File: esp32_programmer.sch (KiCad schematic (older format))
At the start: 5 parts

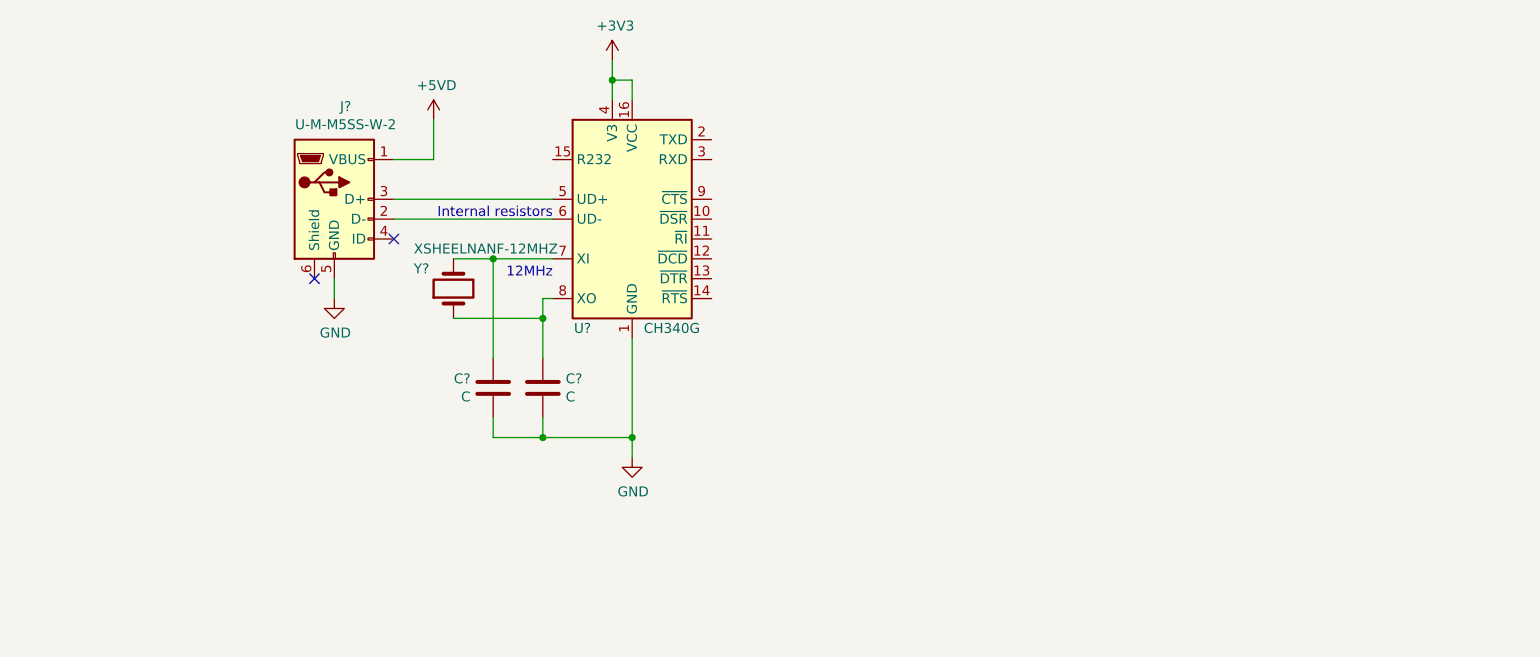
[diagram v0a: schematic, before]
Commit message: corrected capacitors
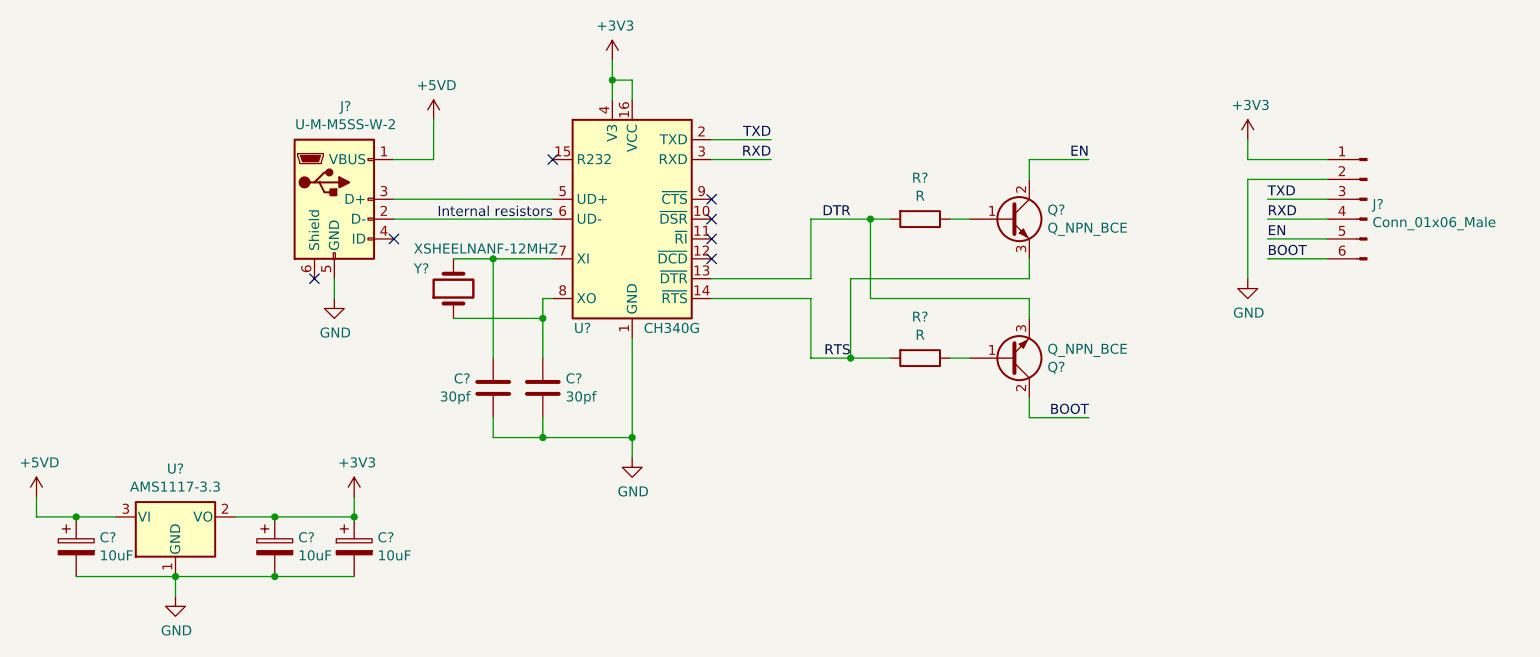
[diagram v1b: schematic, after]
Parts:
- added C? (x3): 10uF, symbol Device:CP
- added J?: Conn_01x06_Male, symbol Connector:Conn_01x06_Male
- added Q? (x2): Q_NPN_BCE, symbol Device:Q_NPN_BCE
- added R? (x2): R, symbol Device:R
- added U?: AMS1117-3.3, Package_TO_SOT_SMD:SOT-223-3_TabPin2, symbol Regulator_Linear:AMS1117-3.3
- C? (x2): value C -> 30pf
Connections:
- net +3V3: now also C?.1, C?.1, J?.1 (Pin_1), U?.2 (VO)
- net +5VD: now also C?.1, U?.3 (VI)
- net GND: now also C?.2, C?.2, C?.2, J?.2 (Pin_2), U?.1 (GND)
- net DTR: now reaches U?.13 (~DTR)
- net DTR: now also Q?.3 (E), R?.2
- net RTS: now reaches U?.14 (~RTS)
- net RTS: now also Q?.3 (E), R?.2
- net TXD: now reaches U?.2 (TXD)
- net TXD: now also J?.3 (Pin_3)
- net RXD: now reaches U?.3 (RXD)
- net RXD: now also J?.4 (Pin_4)
- new net: Q?.1 (B), R?.1 (x2)
- new net BOOT: J?.6 (Pin_6), Q?.2 (C)
- new net EN: J?.5 (Pin_5), Q?.2 (C)
- no-connect marks 2 -> 7
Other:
- note removed: "12MHz"

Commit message: Add project footprints and route PCB
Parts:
- C1, C2, C3: renamed from C?; footprint (none) -> Capacitor_Tantalum_SMD:CP_EIA-3216-18_Kemet-A
- C4, C5: renamed from C?; footprint (none) -> Capacitor_SMD:C_0603_1608Metric
- J1: renamed from J?; value U-M-M5SS-W-2 -> MicroQTJ; footprint (none) -> esp32-programmer:USB_MicroQTJ; LCSC https://lcsc.com/product-detail/USB-Connectors_Korean-Hropa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 -> https://lcsc.com/product-detail/USB-Connectors_SHOU-HAN-Mic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
- J2: renamed from J?; footprint (none) -> Connector_PinHeader_2.54mm:PinHeader_1x06_P2.54mm_Vertical
- Q1, Q2: renamed from Q?; footprint (none) -> Package_TO_SOT_SMD:SOT-23
- R1, R2: renamed from R?; footprint (none) -> Resistor_SMD:R_0603_1608Metric
- Y1: renamed from Y?; footprint (none) -> esp32-programmer:XTAL_XSHEELNANF-12MHZ
- gave numbers to parts that had none: 2
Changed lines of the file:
@@
 $EndDescr
 $Comp
-L Interface_USB:CH340G U?
+L Interface_USB:CH340G U2
 U 1 1 60B77A02
 P 5300 3500
-F 0 "U?" H 5050 2950 50  0000 C CNN
+F 0 "U2" H 5050 2950 50  0000 C CNN
 F 1 "CH340G" H 5500 2950 50  0000 C CNN
 F 2 "Package_SO:SOIC-16_3.9x9.9mm_P1.27mm" H 5350 2950 50  0001 L CNN
@@
 $EndComp
 $Comp
-L Connector:USB_B_Micro J?
+L Connector:USB_B_Micro J1
 U 1 1 60B78CA0
 P 3800 3400
-F 0 "J?" H 3857 3867 50  0000 C CNN
-F 1 "U-M-M5SS-W-2" H 3857 3776 50  0000 C CNN
-F 2 "" H 3950 3350 50  0001 C CNN
+F 0 "J1" H 3857 3867 50  0000 C CNN
+F 1 "MicroQTJ" H 3857 3776 50  0000 C CNN
+F 2 "esp32-programmer:USB_MicroQTJ" H 3950 3350 50  0001 C CNN
 F 3 "~" H 3950 3350 50  0001 C CNN
-F 4 "https://lcsc.com/product-detail/USB-Connectors_Korean-Hroparts-Elec-U-M-M5SS-W-2_C91144.html/?href=jlc-SMT" H 3800 3400 50  0001 C CNN "LCSC"
+F 4 "https://lcsc.com/product-detail/USB-Connectors_SHOU-HAN-MicroQTJ_C404968.html/?href=jlc-SMT" H 3800 3400 50  0001 C CNN "LCSC"
 	1    3800 3400
 	1    0    0    -1
@@
 Internal resistors
 $Comp
-L Device:Crystal Y?
+L Device:Crystal Y1
 U 1 1 60B7C29D
 P 4400 3850
-F 0 "Y?" V 4500 4050 50  0000 R CNN
+F 0 "Y1" V 4500 4050 50  0000 R CNN
 F 1 "XSHEELNANF-12MHZ" V 4600 4050 50  0000 R CNN
-F 2 "" H 4400 3850 50  0001 C CNN
+F 2 "esp32-programmer:XTAL_XSHEELNANF-12MHZ" H 4400 3850 50  0001 C CNN
 F 3 "~" H 4400 3850 50  0001 C CNN
 	1    4400 3850
@@
 	3800 3800 3800 3900
 $Comp
-L power:GND #PWR?
+L power:GND #PWR0101
 U 1 1 60B7FF57
 P 3800 3900
-F 0 "#PWR?" H 3800 3650 50  0001 C CNN
+F 0 "#PWR0101" H 3800 3650 50  0001 C CNN
 F 1 "GND" H 3805 3727 50  0000 C CNN
 F 2 "" H 3800 3900 50  0001 C CNN
@@
 	4300 3200 4300 3000
 $Comp
-L power:+5VD #PWR?
+L power:+5VD #PWR0102
 U 1 1 60B80375
 P 4300 3000
-F 0 "#PWR?" H 4300 2850 50  0001 C CNN
+F 0 "#PWR0102" H 4300 2850 50  0001 C CNN
 F 1 "+5VD" H 4315 3173 50  0000 C CNN
 F 2 "" H 4300 3000 50  0001 C CNN
@@
 $EndComp
 $Comp
-L power:+3V3 #PWR?
+L power:+3V3 #PWR0103
 U 1 1 60B80565
 P 5200 2700
-F 0 "#PWR?" H 5200 2550 50  0001 C CNN
+F 0 "#PWR0103" H 5200 2550 50  0001 C CNN
 F 1 "+3V3" H 5215 2873 50  0000 C CNN
 F 2 "" H 5200 2700 50  0001 C CNN
@@
 	5200 2800 5200 2900
 $Comp
-L power:GND #PWR?
+L power:GND #PWR0104
 U 1 1 60B80D8B
 P 5300 4700
-F 0 "#PWR?" H 5300 4450 50  0001 C CNN
+F 0 "#PWR0104" H 5300 4450 50  0001 C CNN
 F 1 "GND" H 5305 4527 50  0000 C CNN
 F 2 "" H 5300 4700 50  0001 C CNN
@@
 	4850 3900 4900 3900
 $Comp
-L Device:C C?
+L Device:C C4
 U 1 1 60B82D26
 P 4600 4350
-F 0 "C?" H 4486 4304 50  0000 R CNN
+F 0 "C4" H 4486 4304 50  0000 R CNN
 F 1 "30pf" H 4486 4395 50  0000 R CNN
-F 2 "" H 4638 4200 50  0001 C CNN
+F 2 "Capacitor_SMD:C_0603_1608Metric" H 4638 4200 50  0001 C CNN
 F 3 "~" H 4600 4350 50  0001 C CNN
 	1    4600 4350
@@
 $EndComp
 $Comp
-L Device:C C?
+L Device:C C5
 U 1 1 60B83582
 P 4850 4350
-F 0 "C?" H 4965 4396 50  0000 L CNN
+F 0 "C5" H 4965 4396 50  0000 L CNN
 F 1 "30pf" H 4965 4305 50  0000 L CNN
-F 2 "" H 4888 4200 50  0001 C CNN
+F 2 "Capacitor_SMD:C_0603_1608Metric" H 4888 4200 50  0001 C CNN
 F 3 "~" H 4850 4350 50  0001 C CNN
 	1    4850 4350
@@
 NoConn ~ 5700 3400
 $Comp
-L Connector:Conn_01x06_Male J?
+L Connector:Conn_01x06_Male J2
 U 1 1 60B8731F
 P 9000 3400
-F 0 "J?" H 8972 3374 50  0000 R CNN
+F 0 "J2" H 8972 3374 50  0000 R CNN
 F 1 "Conn_01x06_Male" H 8972 3283 50  0000 R CNN
-F 2 "" H 9000 3400 50  0001 C CNN
+F 2 "Connector_PinHeader_2.54mm:PinHeader_1x06_P2.54mm_Vertical" H 9000 3400 50  0001 C CNN
 F 3 "~" H 9000 3400 50  0001 C CNN
 	1    9000 3400
@@
 	5700 3200 6000 3200
 $Comp
-L Device:Q_NPN_BCE Q?
+L Device:Q_NPN_BCE Q1
 U 1 1 60B8D21D
 P 7200 3500
-F 0 "Q?" H 7391 3546 50  0000 L CNN
+F 0 "Q1" H 7391 3546 50  0000 L CNN
 F 1 "Q_NPN_BCE" H 7391 3455 50  0000 L CNN
-F 2 "" H 7400 3600 50  0001 C CNN
+F 2 "Package_TO_SOT_SMD:SOT-23" H 7400 3600 50  0001 C CNN
 F 3 "~" H 7200 3500 50  0001 C CNN
 	1    7200 3500
@@
 $EndComp
 $Comp
-L Device:Q_NPN_BCE Q?
+L Device:Q_NPN_BCE Q2
 U 1 1 60B8DFFF
 P 7200 4200
-F 0 "Q?" H 7391 4246 50  0000 L CNN
+F 0 "Q2" H 7391 4246 50  0000 L CNN
 F 1 "Q_NPN_BCE" H 7391 4155 50  0000 L CNN
-F 2 "" H 7400 4300 50  0001 C CNN
+F 2 "Package_TO_SOT_SMD:SOT-23" H 7400 4300 50  0001 C CNN
 F 3 "~" H 7200 4200 50  0001 C CNN
 	1    7200 4200
@@
 $EndComp
 $Comp
-L Device:R R?
+L Device:R R1
 U 1 1 60B8FD55
 P 6750 3500
-F 0 "R?" V 6543 3500 50  0000 C CNN
+F 0 "R1" V 6543 3500 50  0000 C CNN
 F 1 "R" V 6634 3500 50  0000 C CNN
-F 2 "" V 6680 3500 50  0001 C CNN
+F 2 "Resistor_SMD:R_0603_1608Metric" V 6680 3500 50  0001 C CNN
 F 3 "~" H 6750 3500 50  0001 C CNN
 	1    6750 3500
@@
 $EndComp
 $Comp
-L Device:R R?
+L Device:R R2
 U 1 1 60B902CA
 P 6750 4200
-F 0 "R?" V 6543 4200 50  0000 C CNN
+F 0 "R2" V 6543 4200 50  0000 C CNN
 F 1 "R" V 6634 4200 50  0000 C CNN
-F 2 "" V 6680 4200 50  0001 C CNN
+F 2 "Resistor_SMD:R_0603_1608Metric" V 6680 4200 50  0001 C CNN
 F 3 "~" H 6750 4200 50  0001 C CNN
 	1    6750 4200
@@
 BOOT
 $Comp
-L Regulator_Linear:AMS1117-3.3 U?
+L Regulator_Linear:AMS1117-3.3 U1
 U 1 1 60A3C5EF
 P 3000 5000
-F 0 "U?" H 3000 5242 50  0000 C CNN
+F 0 "U1" H 3000 5242 50  0000 C CNN
 F 1 "AMS1117-3.3" H 3000 5151 50  0000 C CNN
 F 2 "Package_TO_SOT_SMD:SOT-223-3_TabPin2" H 3000 5200 50  0001 C CNN
@@
 $EndComp
 $Comp
-L power:+5VD #PWR?
+L power:+5VD #PWR0105
 U 1 1 60A436C2
 P 2300 4900
-F 0 "#PWR?" H 2300 4750 50  0001 C CNN
+F 0 "#PWR0105" H 2300 4750 50  0001 C CNN
 F 1 "+5VD" H 2315 5073 50  0000 C CNN
 F 2 "" H 2300 4900 50  0001 C CNN
@@
 $EndComp
 $Comp
-L power:+3V3 #PWR?
+L power:+3V3 #PWR0106
 U 1 1 60A43EF7
 P 3900 4900
-F 0 "#PWR?" H 3900 4750 50  0001 C CNN
+F 0 "#PWR0106" H 3900 4750 50  0001 C CNN
 F 1 "+3V3" H 3915 5073 50  0000 C CNN
 F 2 "" H 3900 4900 50  0001 C CNN
@@
 	3000 5400 3000 5300
 $Comp
-L power:GND #PWR?
+L power:GND #PWR0107
 U 1 1 60A4DA75
 P 3000 5400
-F 0 "#PWR?" H 3000 5150 50  0001 C CNN
+F 0 "#PWR0107" H 3000 5150 50  0001 C CNN
 F 1 "GND" H 3005 5227 50  0000 C CNN
 F 2 "" H 3000 5400 50  0001 C CNN
@@
 	8500 3700 8800 3700
 $Comp
-L power:+3V3 #PWR?
+L power:+3V3 #PWR0108
 U 1 1 60A5CA6C
 P 8400 3100
-F 0 "#PWR?" H 8400 2950 50  0001 C CNN
+F 0 "#PWR0108" H 8400 2950 50  0001 C CNN
 F 1 "+3V3" H 8415 3273 50  0000 C CNN
 F 2 "" H 8400 3100 50  0001 C CNN
@@
 $EndComp
 $Comp
-L power:GND #PWR?
+L power:GND #PWR0109
 U 1 1 60A5D1AC
 P 8400 3800
-F 0 "#PWR?" H 8400 3550 50  0001 C CNN
+F 0 "#PWR0109" H 8400 3550 50  0001 C CNN
 F 1 "GND" H 8405 3627 50  0000 C CNN
 F 2 "" H 8400 3800 50  0001 C CNN
@@
 	2300 5000 2500 5000
 $Comp
-L Device:CP C?
+L Device:CP C1
 U 1 1 60A3D7DA
 P 2500 5150
-F 0 "C?" H 2618 5196 50  0000 L CNN
+F 0 "C1" H 2618 5196 50  0000 L CNN
 F 1 "10uF" H 2618 5105 50  0000 L CNN
-F 2 "" H 2538 5000 50  0001 C CNN
+F 2 "Capacitor_Tantalum_SMD:CP_EIA-3216-18_Kemet-A" H 2538 5000 50  0001 C CNN
 F 3 "~" H 2500 5150 50  0001 C CNN
 	1    2500 5150
@@
 	2500 5000 2700 5000
 $Comp
-L Device:CP C?
+L Device:CP C3
 U 1 1 60A3ED44
 P 3900 5150
-F 0 "C?" H 4018 5196 50  0000 L CNN
+F 0 "C3" H 4018 5196 50  0000 L CNN
 F 1 "10uF" H 4018 5105 50  0000 L CNN
-F 2 "" H 3938 5000 50  0001 C CNN
+F 2 "Capacitor_Tantalum_SMD:CP_EIA-3216-18_Kemet-A" H 3938 5000 50  0001 C CNN
 F 3 "~" H 3900 5150 50  0001 C CNN
 	1    3900 5150
@@
 Connection ~ 3900 5000
 $Comp
-L Device:CP C?
+L Device:CP C2
 U 1 1 60A3F0B8
 P 3500 5150
-F 0 "C?" H 3618 5196 50  0000 L CNN
+F 0 "C2" H 3618 5196 50  0000 L CNN
 F 1 "10uF" H 3618 5105 50  0000 L CNN
-F 2 "" H 3538 5000 50  0001 C CNN
+F 2 "Capacitor_Tantalum_SMD:CP_EIA-3216-18_Kemet-A" H 3538 5000 50  0001 C CNN
 F 3 "~" H 3500 5150 50  0001 C CNN
 	1    3500 5150

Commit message: Created BOM, Gerbers and pos files. RFM.
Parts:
- C1, C2, C3: LCSC (none) -> C7171
- C4, C5: LCSC (none) -> C22397
- J1: LCSC https://lcsc.com/product-detail/USB-Connectors_SHOU-HAN-Mic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 -> C404968
- J2: LCSC (none) -> C124380
- Q1, Q2: value Q_NPN_BCE -> SS8050; LCSC (none) -> C2150
- R1, R2: value R -> 12k; LCSC (none) -> C22790
- U1: LCSC (none) -> C6186
- U2: LCSC (none) -> C14267
- Y1: LCSC (none) -> C295065
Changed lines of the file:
@@
 F 2 "Package_SO:SOIC-16_3.9x9.9mm_P1.27mm" H 5350 2950 50  0001 L CNN
 F 3 "http://www.datasheet5.com/pdf-local-2195953" H 4950 4300 50  0001 C CNN
+F 4 "C14267" H 5300 3500 50  0001 C CNN "LCSC"
 	1    5300 3500
 	1    0    0    -1
@@
 F 2 "esp32-programmer:USB_MicroQTJ" H 3950 3350 50  0001 C CNN
 F 3 "~" H 3950 3350 50  0001 C CNN
-F 4 "https://lcsc.com/product-detail/USB-Connectors_SHOU-HAN-MicroQTJ_C404968.html/?href=jlc-SMT" H 3800 3400 50  0001 C CNN "LCSC"
+F 4 "C404968" H 3800 3400 50  0001 C CNN "LCSC"
 	1    3800 3400
 	1    0    0    -1
@@
 F 2 "esp32-programmer:XTAL_XSHEELNANF-12MHZ" H 4400 3850 50  0001 C CNN
 F 3 "~" H 4400 3850 50  0001 C CNN
+F 4 "C295065" H 4400 3850 50  0001 C CNN "LCSC"
 	1    4400 3850
 	0    -1   -1   0
@@
 F 2 "Capacitor_SMD:C_0603_1608Metric" H 4638 4200 50  0001 C CNN
 F 3 "~" H 4600 4350 50  0001 C CNN
+F 4 "C22397" H 4600 4350 50  0001 C CNN "LCSC"
 	1    4600 4350
 	1    0    0    1
@@
 F 2 "Capacitor_SMD:C_0603_1608Metric" H 4888 4200 50  0001 C CNN
 F 3 "~" H 4850 4350 50  0001 C CNN
+F 4 "C22397" H 4850 4350 50  0001 C CNN "LCSC"
 	1    4850 4350
 	1    0    0    -1
@@
 F 2 "Connector_PinHeader_2.54mm:PinHeader_1x06_P2.54mm_Vertical" H 9000 3400 50  0001 C CNN
 F 3 "~" H 9000 3400 50  0001 C CNN
+F 4 "C124380" H 9000 3400 50  0001 C CNN "LCSC"
 	1    9000 3400
 	-1   0    0    -1
@@
 P 7200 3500
 F 0 "Q1" H 7391 3546 50  0000 L CNN
-F 1 "Q_NPN_BCE" H 7391 3455 50  0000 L CNN
+F 1 "SS8050" H 7391 3455 50  0000 L CNN
 F 2 "Package_TO_SOT_SMD:SOT-23" H 7400 3600 50  0001 C CNN
 F 3 "~" H 7200 3500 50  0001 C CNN
+F 4 "C2150" H 7200 3500 50  0001 C CNN "LCSC"
 	1    7200 3500
 	1    0    0    -1
@@
 P 7200 4200
 F 0 "Q2" H 7391 4246 50  0000 L CNN
-F 1 "Q_NPN_BCE" H 7391 4155 50  0000 L CNN
+F 1 "SS8050" H 7391 4155 50  0000 L CNN
 F 2 "Package_TO_SOT_SMD:SOT-23" H 7400 4300 50  0001 C CNN
 F 3 "~" H 7200 4200 50  0001 C CNN
+F 4 "C2150" H 7200 4200 50  0001 C CNN "LCSC"
 	1    7200 4200
 	1    0    0    1
@@
 P 6750 3500
 F 0 "R1" V 6543 3500 50  0000 C CNN
-F 1 "R" V 6634 3500 50  0000 C CNN
+F 1 "12k" V 6634 3500 50  0000 C CNN
 F 2 "Resistor_SMD:R_0603_1608Metric" V 6680 3500 50  0001 C CNN
 F 3 "~" H 6750 3500 50  0001 C CNN
+F 4 "C22790" H 6750 3500 50  0001 C CNN "LCSC"
 	1    6750 3500
 	0    1    1    0
@@
 P 6750 4200
 F 0 "R2" V 6543 4200 50  0000 C CNN
-F 1 "R" V 6634 4200 50  0000 C CNN
+F 1 "12k" V 6634 4200 50  0000 C CNN
 F 2 "Resistor_SMD:R_0603_1608Metric" V 6680 4200 50  0001 C CNN
 F 3 "~" H 6750 4200 50  0001 C CNN
+F 4 "C22790" H 6750 4200 50  0001 C CNN "LCSC"
 	1    6750 4200
 	0    1    1    0
@@
 F 2 "Package_TO_SOT_SMD:SOT-223-3_TabPin2" H 3000 5200 50  0001 C CNN
 F 3 "http://www.advanced-monolithic.com/pdf/ds1117.pdf" H 3100 4750 50  0001 C CNN
+F 4 "C6186" H 3000 5000 50  0001 C CNN "LCSC"
 	1    3000 5000
 	1    0    0    -1
@@
 F 2 "Capacitor_Tantalum_SMD:CP_EIA-3216-18_Kemet-A" H 2538 5000 50  0001 C CNN
 F 3 "~" H 2500 5150 50  0001 C CNN
+F 4 "C7171" H 2500 5150 50  0001 C CNN "LCSC"
 	1    2500 5150
 	1    0    0    -1
@@
 F 2 "Capacitor_Tantalum_SMD:CP_EIA-3216-18_Kemet-A" H 3938 5000 50  0001 C CNN
 F 3 "~" H 3900 5150 50  0001 C CNN
+F 4 "C7171" H 3900 5150 50  0001 C CNN "LCSC"
 	1    3900 5150
 	1    0    0    -1
@@
 F 2 "Capacitor_Tantalum_SMD:CP_EIA-3216-18_Kemet-A" H 3538 5000 50  0001 C CNN
 F 3 "~" H 3500 5150 50  0001 C CNN
+F 4 "C7171" H 3500 5150 50  0001 C CNN "LCSC"
 	1    3500 5150
 	1    0    0    -1
